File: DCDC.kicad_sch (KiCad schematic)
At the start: 23 parts, among them U5 LM76005RNPR

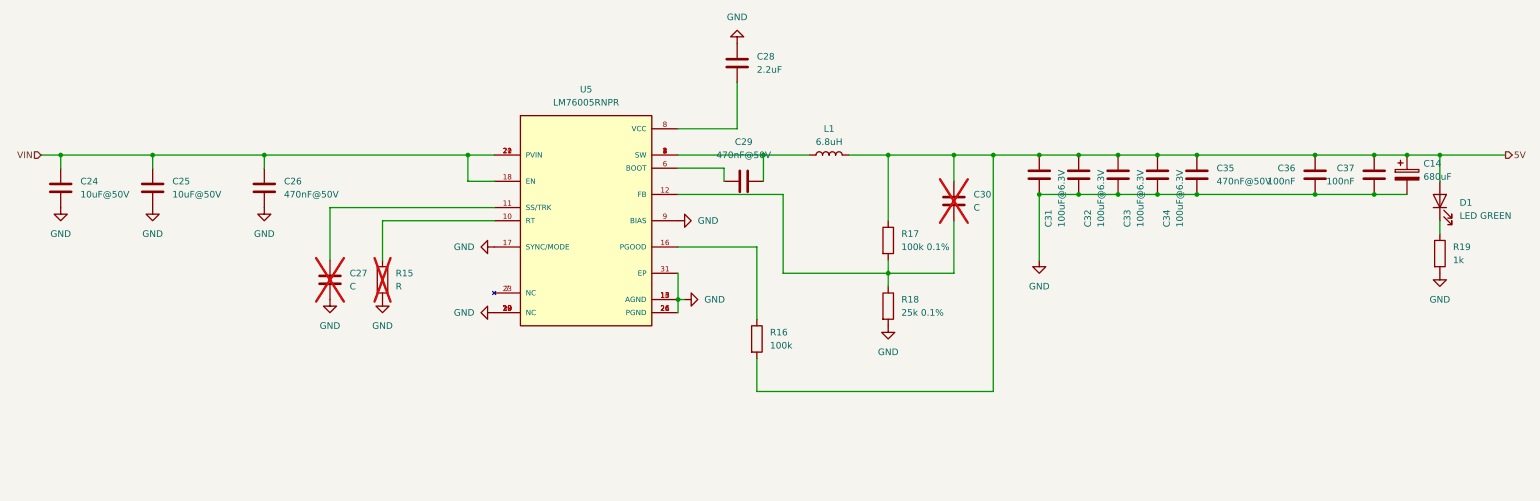
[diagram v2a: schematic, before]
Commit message: Added bias supply to DCDC for improved efficiency
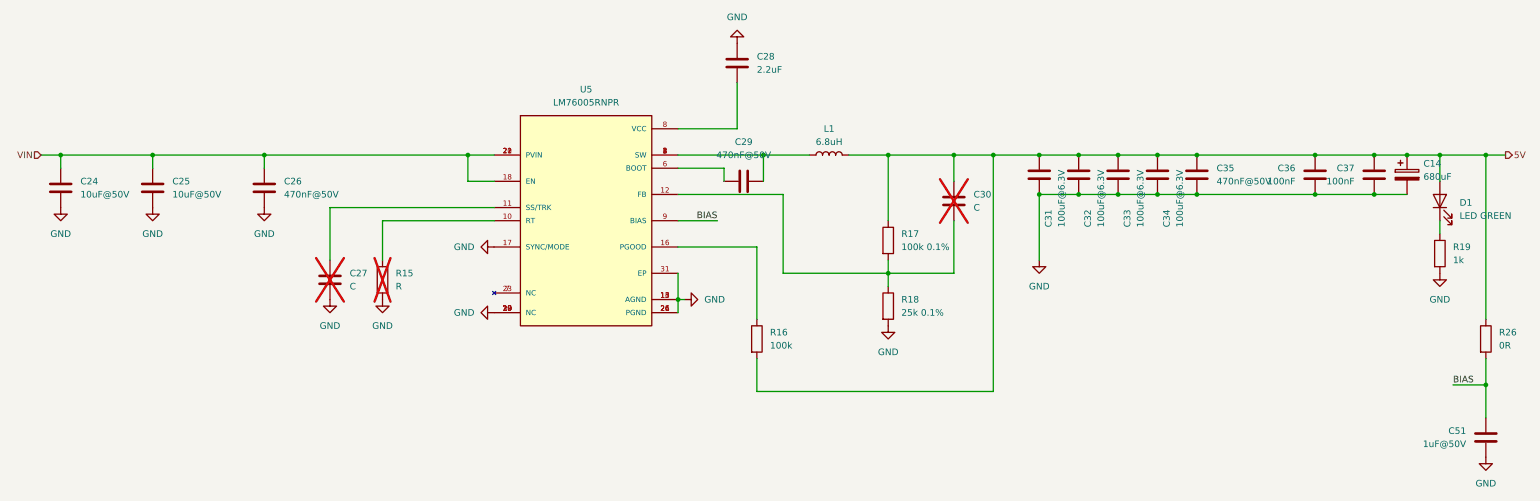
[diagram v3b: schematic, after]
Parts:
- added C51: 1uF@50V, Capacitor_SMD:C_0805_2012Metric, symbol Device:C
- added R26: 0R, Resistor_SMD:R_0805_2012Metric, symbol Device:R
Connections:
- net 5V: now also R26.1
- net GND: now also C51.1; no longer U5.9 (BIAS)
- new net BIAS: C51.2, R26.2, U5.9 (BIAS)

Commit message: Make ERC happy
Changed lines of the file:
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@@
 (kicad_sch
-	(version 20231120)
+	(version 20250114)
 	(generator "eeschema")
-	(generator_version "8.0")
+	(generator_version "9.0")
 	(paper "A3")
 	(junction
@@
 	(label "BIAS"
 		(at 203.2 140.97 180)
-		(fields_autoplaced yes)
 		(effects
 			(font
@@
 	(label "BIAS"
 		(at 345.44 172.72 0)
-		(fields_autoplaced yes)
 		(effects
 			(font
@@
 		(shape input)
 		(at 72.39 128.27 180)
-		(fields_autoplaced yes)
 		(effects
 			(font
@@
 		(shape output)
 		(at 355.6 128.27 0)
-		(fields_autoplaced yes)
 		(effects
 			(font
@@
 			(at 342.9 137.16 0)
 			(effects
+				(font
+					(size 1.27 1.27)
+				)
+				(hide yes)
+			)
+		)
+		(property "Sim.Pins" "1=K 2=A"
+			(at 342.9 137.16 0)
+			(effects

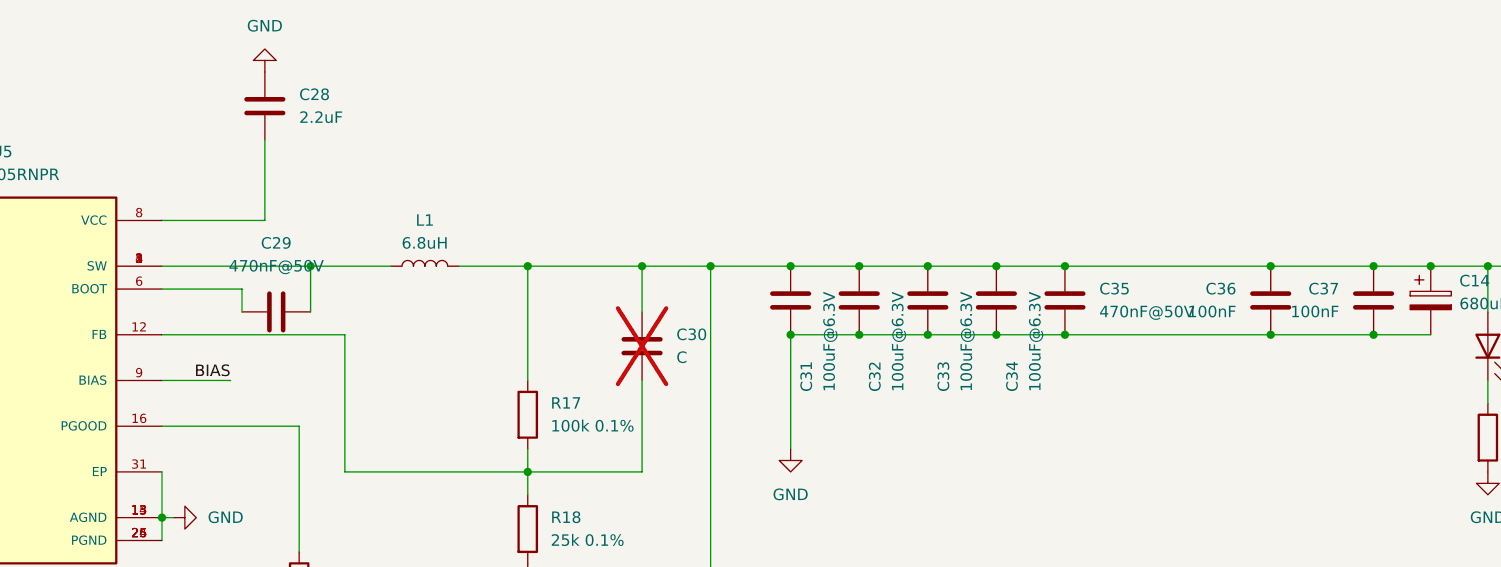
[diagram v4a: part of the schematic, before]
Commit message: Fix BOM and switch C0402 to C0603
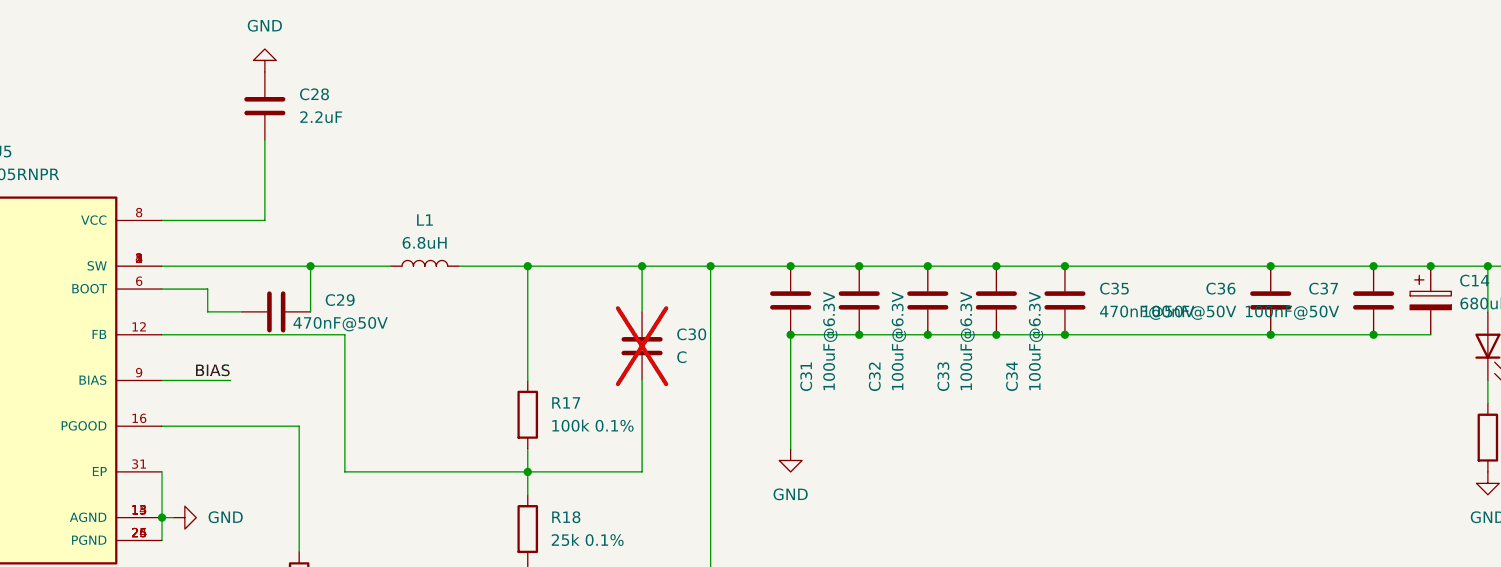
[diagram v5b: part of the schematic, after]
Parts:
- C36, C37: value 100nF -> 100nF@50V; footprint Capacitor_SMD:C_0402_1005Metric -> Capacitor_SMD:C_0603_1608Metric; JLC C307331 -> C14663
- R17: footprint Resistor_SMD:R_0805_2012Metric -> Resistor_SMD:R_0603_1608Metric; JLC C149504 -> C122538
- R18: footprint Resistor_SMD:R_0805_2012Metric -> Resistor_SMD:R_0603_1608Metric; JLC C153306 -> C2828637
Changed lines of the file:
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@@
 	(wire
 		(pts
-			(xy 204.47 130.81) (xy 204.47 133.35)
+			(xy 200.66 130.81) (xy 200.66 133.35)
 		)
 		(stroke
@@
 	(wire
 		(pts
-			(xy 195.58 130.81) (xy 204.47 130.81)
+			(xy 195.58 130.81) (xy 200.66 130.81)
 		)
 		(stroke
@@
 	(wire
 		(pts
+			(xy 200.66 133.35) (xy 204.47 133.35)
+		)
+		(stroke
+			(width 0)
+			(type default)
+		)
+	)
+	(wire
+		(pts
 			(xy 265.43 135.89) (xy 265.43 148.59)
 		)
@@
 			)
 		)
-		(property "Value" "100nF"
+		(property "Value" "100nF@50V"
 			(at 326.39 133.3499 0)
 			(effects
@@
 			)
 		)
-		(property "Footprint" "Capacitor_SMD:C_0402_1005Metric"
+		(property "Footprint" "Capacitor_SMD:C_0603_1608Metric"
 			(at 331.1652 128.27 0)
 			(effects
@@
 			)
 		)
-		(property "JLC" "C307331"
+		(property "JLC" "C14663"
 			(at 330.2 132.08 0)
 			(effects
@@
 			)
 		)
-		(property "Footprint" "Resistor_SMD:R_0805_2012Metric"
+		(property "Footprint" "Resistor_SMD:R_0603_1608Metric"
 			(at 234.442 157.48 90)
 			(effects
@@
 			)
 		)
-		(property "JLC" "C153306"
+		(property "JLC" "C2828637"
 			(at 236.22 157.48 0)
 			(effects
@@
 		(on_board yes)
 		(dnp no)
-		(fields_autoplaced yes)
 		(property "Reference" "C29"
-			(at 208.28 125.73 90)
+			(at 215.392 132.08 90)
 			(effects
 				(font
@@
 		)
 		(property "Value" "470nF@50V"
-			(at 208.28 128.27 90)
+			(at 215.392 134.62 90)
 			(effects
 				(font
@@
 			)
 		)
-		(property "Value" "100nF"
+		(property "Value" "100nF@50V"
 			(at 314.96 133.3499 0)
 			(effects
@@
 			)
 		)
-		(property "Footprint" "Capacitor_SMD:C_0402_1005Metric"
+		(property "Footprint" "Capacitor_SMD:C_0603_1608Metric"
 			(at 319.7352 128.27 0)
 			(effects
@@
 			)
 		)
-		(property "JLC" "C307331"
+		(property "JLC" "C14663"
 			(at 318.77 132.08 0)
 			(effects
@@
 			)
 		)
-		(property "Footprint" "Resistor_SMD:R_0805_2012Metric"
+		(property "Footprint" "Resistor_SMD:R_0603_1608Metric"
 			(at 234.442 144.78 90)
 			(effects
@@
 			)
 		)
-		(property "JLC" "C149504"
+		(property "JLC" "C122538"
 			(at 236.22 144.78 0)
 			(effects
